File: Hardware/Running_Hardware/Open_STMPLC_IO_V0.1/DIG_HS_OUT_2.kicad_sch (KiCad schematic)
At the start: 24 parts, among them J13 Screw_Terminal_01x02, Q1 2N7002K, U14 TPS26600PWP, U15 NVTFS5124PLTAG

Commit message: Analog input section
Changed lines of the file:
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@@
 			(effects
 				(font
-					(size 1.27 1.27)
+					(size 1 1)
 				)
 				(justify left)
@@
 			(effects
 				(font
-					(size 1.27 1.27)
+					(size 1 1)
 				)
 				(justify left)
@@
 			(effects
 				(font
-					(size 1.27 1.27)
+					(size 1 1)
 				)
 				(justify left)
@@
 			(effects
 				(font
-					(size 1.27 1.27)
+					(size 1 1)
 				)
 				(justify left)

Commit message: GSM Module add
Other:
- title: (none) -> Open_PLC_IO
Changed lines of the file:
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@@
 	(generator_version "9.0")
 	(paper "A4")
+	(title_block
+		(title "Open_PLC_IO")
+		(date "2026-04-01")
+		(rev "0.1")
+	)
 	(rectangle
 		(start 13.97 13.97)

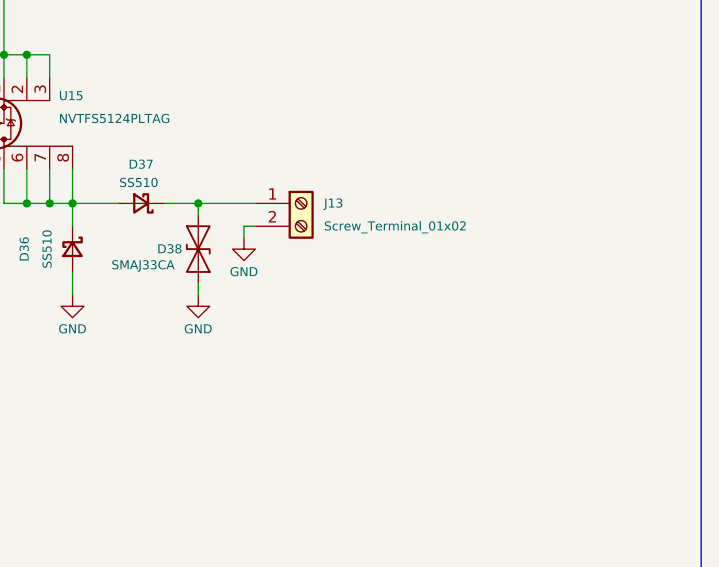
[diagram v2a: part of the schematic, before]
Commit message: Main PCB schematic changes V0.1
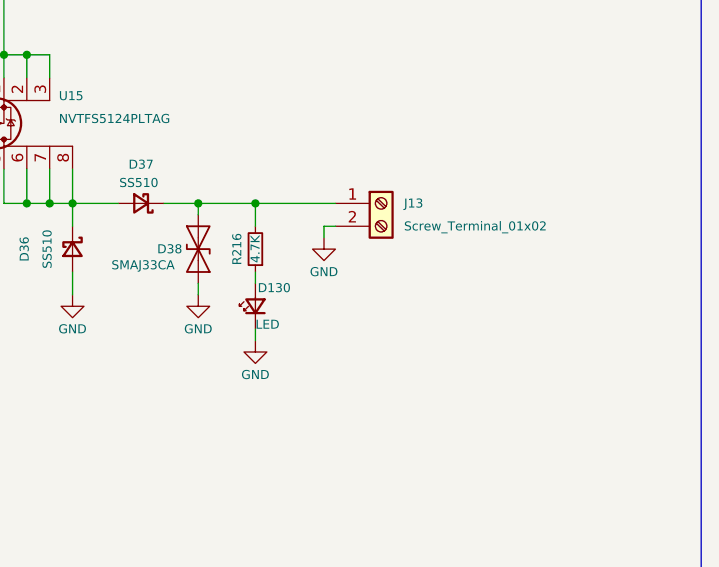
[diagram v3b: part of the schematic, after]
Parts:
- added D130: LED, LED_SMD:LED_0603_1608Metric_Pad1.05x0.95mm_HandSolder, symbol Device:LED_Small
- added R216: 4.7K, Resistor_SMD:R_0603_1608Metric_Pad0.98x0.95mm_HandSolder, symbol Device:R_Small
- C23, C24, C26: footprint (none) -> Capacitor_SMD:C_0603_1608Metric_Pad1.08x0.95mm_HandSolder
- C25: footprint (none) -> Capacitor_SMD:C_0805_2012Metric_Pad1.18x1.45mm_HandSolder
- D35: footprint (none) -> Diode_SMD:D_SOD-123
- J13: footprint (none) -> TerminalBlock_Phoenix:TerminalBlock_Phoenix_MKDS-1,5-2_1x02_P5.00mm_Horizontal
- R87, R88, R89, R90: footprint (none) -> Resistor_SMD:R_0603_1608Metric_Pad0.98x0.95mm_HandSolder
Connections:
- net GND: now also D130.1 (K)
- net at D37.1 (K), D38.1 (A1), J13.1 (Pin_1): now also R216.2
- new net: D130.2 (A), R216.1
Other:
- title: Open_PLC_IO -> Open_STMPLC_IO
- moved on the sheet: J13

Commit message: New DXF update
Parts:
- J13: footprint TerminalBlock_Phoenix:TerminalBlock_Phoenix_MKDS-1,5-2_1x02_P5.00mm_Horizontal -> TerminalBlock_Phoenix:TerminalBlock_Phoenix_MKDS-1-2-3.81_1x02_P3.81mm_Horizontal
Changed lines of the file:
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@@
 			)
 		)
-		(property "Footprint" "TerminalBlock_Phoenix:TerminalBlock_Phoenix_MKDS-1,5-2_1x02_P5.00mm_Horizontal"
+		(property "Footprint" "TerminalBlock_Phoenix:TerminalBlock_Phoenix_MKDS-1-2-3.81_1x02_P3.81mm_Horizontal"
 			(at 246.38 88.9 0)
 			(effects

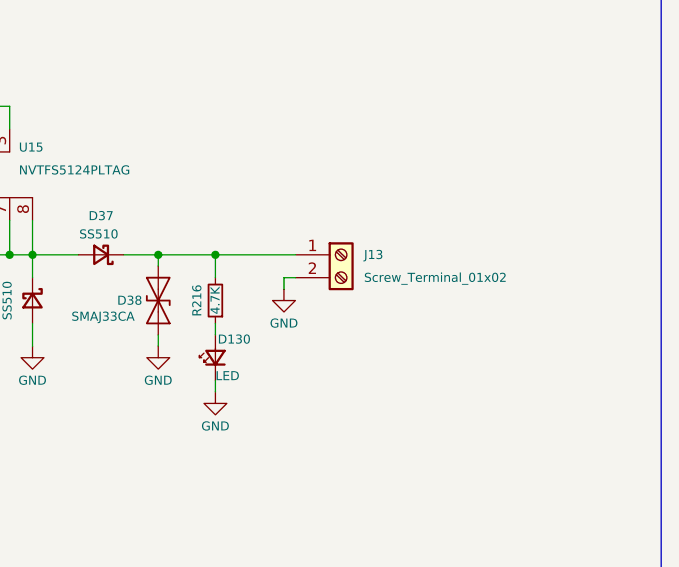
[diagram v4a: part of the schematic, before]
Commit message: Common GND terminal changes
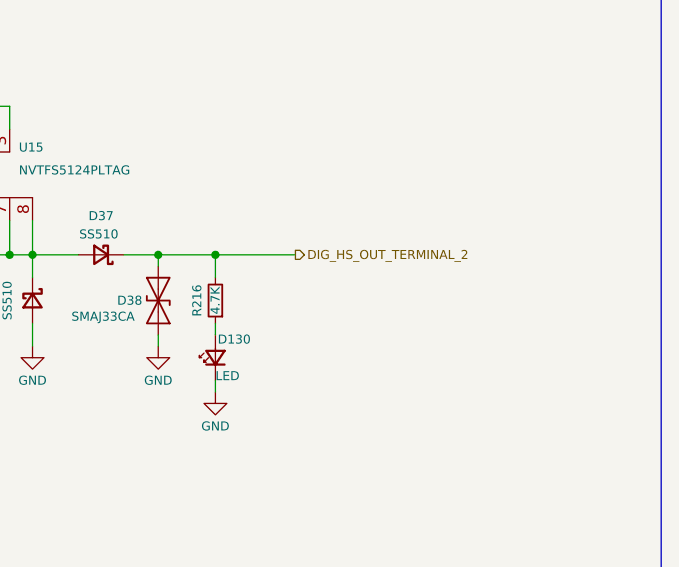
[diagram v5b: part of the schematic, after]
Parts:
- removed J13: Screw_Terminal_01x02, TerminalBlock_Phoenix:TerminalBlock_Phoenix_MKDS-1-2-3.81_1x02_P3.81mm_Horizontal, symbol Connector:Screw_Terminal_01x02
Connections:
- net DIG_HS_OUT_TERMINAL_2: now reaches D37.1 (K), D38.1 (A1), R216.2
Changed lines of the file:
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@@
-	(wire
-		(pts
-			(xy 240.03 92.71) (xy 240.03 91.44)
-		)
-		(stroke
-			(width 0)
-			(type default)
-		)
-	)
 	(wire
 		(pts
@@
 	(wire
 		(pts
-			(xy 240.03 91.44) (xy 241.3 91.44)
-		)
-		(stroke
-			(width 0)
-			(type default)
-		)
-	)
-	(wire
-		(pts
 			(xy 189.23 80.01) (xy 193.04 80.01)
 		)
@@
 			(width 0)
 			(type default)
+		)
+	)
+	(hierarchical_label "DIG_HS_OUT_TERMINAL_2"
+		(shape output)
+		(at 241.3 88.9 0)
+		(effects
+			(font
+				(size 1 1)
+			)
+			(justify left)
 		)
 	)
@@
 				(path "/4d6787b6-1f4f-4098-b70b-d936e584350b/dbe29928-7395-4ef9-a75f-9ae2dbfd9b50"
 					(reference "#PWR083")
-					(unit 1)
-				)
-			)
-		)
-	)
-	(symbol
-		(lib_id "Connector:Screw_Terminal_01x02")
-		(at 246.38 88.9 0)
-		(unit 1)
-		(exclude_from_sim no)
-		(in_bom yes)
-		(on_board yes)
-		(dnp no)
-		(fields_autoplaced yes)
-		(property "Reference" "J13"
-			(at 248.92 88.8999 0)
-			(effects
-				(font
-					(size 1 1)
-				)
-				(justify left)
-			)
-		)
-		(property "Value" "Screw_Terminal_01x02"
-			(at 248.92 91.4399 0)
-			(effects
-				(font
-					(size 1 1)
-				)
-				(justify left)
-			)
-		)
-		(property "Footprint" "TerminalBlock_Phoenix:TerminalBlock_Phoenix_MKDS-1-2-3.81_1x02_P3.81mm_Horizontal"
-			(at 246.38 88.9 0)
-			(effects
-				(font
-					(size 1.27 1.27)
-				)
-				(hide yes)
-			)
-		)
-		(property "Datasheet" "~"
-			(at 246.38 88.9 0)
-			(effects
-				(font
-					(size 1.27 1.27)
-				)
-				(hide yes)
-			)
-		)
-		(property "Description" "Generic screw terminal, single row, 01x02, script generated (kicad-library-utils/schlib/autogen/connector/)"
-			(at 246.38 88.9 0)
-			(effects
-				(font
-					(size 1.27 1.27)
-				)
-				(hide yes)
-			)
-		)
-		(pin "1"
-		)
-		(pin "2"
-		)
-		(instances
-			(project "Open_STMPLC_IO_V0.1"
-				(path "/4d6787b6-1f4f-4098-b70b-d936e584350b/dbe29928-7395-4ef9-a75f-9ae2dbfd9b50"
-					(reference "J13")
 					(unit 1)
 				)
@@
 					(unit 1)
 				)
-			)
-		)
-	)
-	(symbol
-		(lib_id "power:GND")
-		(at 240.03 92.71 0)
-		(unit 1)
-		(exclude_from_sim no)
-		(in_bom yes)
-		(on_board yes)
-		(dnp no)
-		(property "Reference" "#PWR088"
-			(at 240.03 99.06 0)
-			(effects
-				(font
-					(size 1 1)
-				)
-				(hide yes)
-			)
-		)
-		(property "Value" "GND"
-			(at 240.03 96.52 0)
-			(effects
-				(font
-					(size 1 1)
-				)
-			)
-		)
-		(property "Footprint" ""
-			(at 240.03 92.71 0)
-			(effects
-				(font
-					(size 1.27 1.27)
-				)
-				(hide yes)
-			)
-		)
-		(property "Datasheet" ""
-			(at 240.03 92.71 0)
-			(effects
-				(font
-					(size 1.27 1.27)
-				)
-				(hide yes)
-			)
-		)
-		(property "Description" "Power symbol creates a global label with name \"GND\" , ground"
-			(at 240.03 92.71 0)
-			(effects
-				(font
-					(size 1.27 1.27)
-				)
-				(hide yes)
-			)
-		)
-		(pin "1"
-		)
-		(instances
-			(project "Open_STMPLC_IO_V0.1"
-				(path "/4d6787b6-1f4f-4098-b70b-d936e584350b/dbe29928-7395-4ef9-a75f-9ae2dbfd9b50"
-					(reference "#PWR088")
-					(unit 1)
-				)

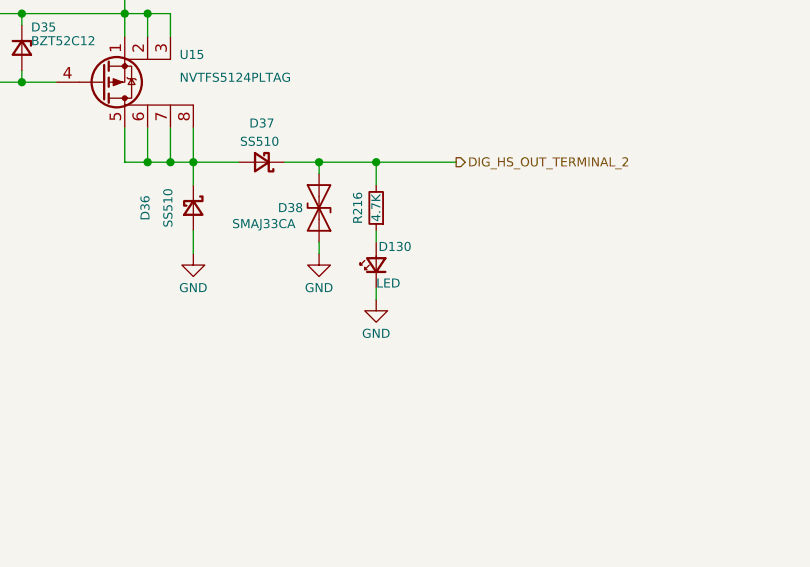
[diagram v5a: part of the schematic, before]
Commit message: Schematic updates
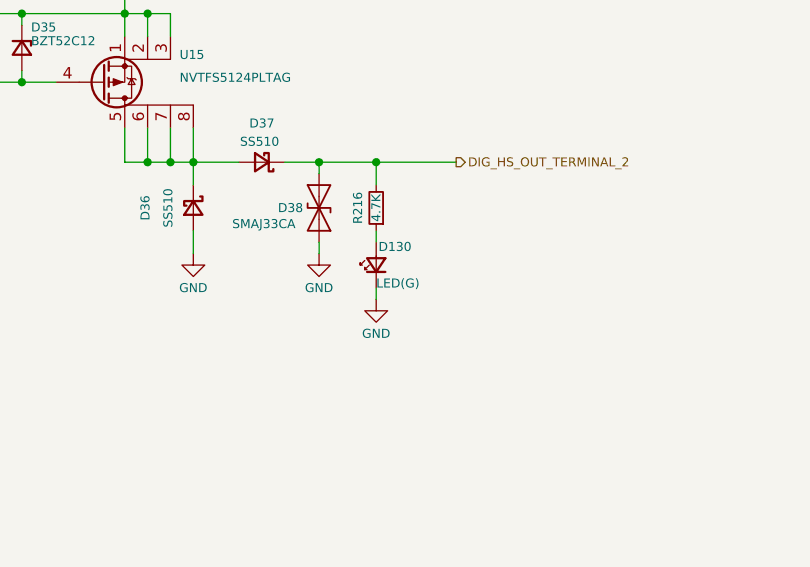
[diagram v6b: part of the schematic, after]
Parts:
- D130: value LED -> LED(G)
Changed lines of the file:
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@@
 			)
 		)
-		(property "Value" "LED"
+		(property "Value" "LED(G)"
 			(at 232.41 102.362 90)
 			(effects

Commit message: Gerber generation v0.1
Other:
- company: (none) -> Thingslista Automation LLP
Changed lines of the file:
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@@
 	(title_block
 		(title "Open_STMPLC_IO")
-		(date "2026-05-23")
+		(date "2026-06-03")
 		(rev "0.1")
+		(company "Thingslista Automation LLP")
 	)
 	(rectangle
